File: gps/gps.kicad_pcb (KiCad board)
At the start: 2 copper layers, 167 x 82.5 mm, 62 parts, among them J1 I2C/BATT_H, J12 ENC+RGB, J13 ENC+RGB, J2 I2C/BATT_S, J3 USB_pads, J4 BATT, J5 ESP, J7 USB_B_Micro, J9 USB_pads, SW1 RotaryEncoder_Switch, SW2 SW_DPDT_x2, U1 NEO-M9N, U10 24C32, U2 TPS613222ADBVR, U3 DFR0654, U4 HT16k33, U5 7seg_1x1_rgb, U6 7seg_1x1_rgb, U7 7seg_1x1_rgb, U8 KW4-804AGB

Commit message: tweaks
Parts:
- J7: footprint Connector_USB:USB_Mini-B_Tensility_54-00023_Vertical_CircularHoles -> KiCad:USB3145301A
- REF** (x3): value MountingHole_3.2mm_M3 -> MountingHole_4.3mm_M4; footprint MountingHole:MountingHole_3.2mm_M3 -> MountingHole:MountingHole_4.3mm_M4
- SW2: value SW_DPDT_x2 -> MSN22AFW01
- moved AE1 17.9 mm to (213.8, 105.4), turned to 90 degrees
- moved J3 14.2 mm to (216.8, 95.3), turned to 90 degrees
- moved J5 10.4 mm to (146.7, 61.4), turned to 90 degrees
- moved C3 10.2 mm to (208.6, 101.2), turned to -90 degrees
- moved R_E3 10.1 mm to (63.1, 120.0)
- moved L1 9.90 mm to (208.6, 104.4), turned to 90 degrees
- moved R2 8.00 mm to (206.3, 101.0), turned to -90 degrees
- moved C1 7.34 mm to (193.4, 89.3)
- moved C2 7.34 mm to (189.7, 92.7)
- moved U1 7.34 mm to (197.7, 99.5)
- moved R_E2 6.35 mm to (67.0, 118.3), turned to -90 degrees
- moved R_E1 3.58 mm to (70.9, 109.3)
- moved J7 1.62 mm to (84.3, 49.2)
- moved D2 0.41 mm to (67.7, 70.9)
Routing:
- net SW_ESP: track 147.2 -> 136.9 mm
- net SW: track 88.9 -> 78.7 mm
- net GNSS_RXD: track 55.1 -> 65.0 mm
- net GNSS_TXD: track 44.0 -> 52.1 mm
- net Net-(J3-Pin_2): track 4.73 -> 12.4 mm
- net Net-(U1-VCC_RF): track 2.70 -> 9.01 mm
- net PULSE: track 26.5 -> 31.7 mm
- net Net-(J3-Pin_3): track 5.51 -> 10.7 mm
- net +3V3: track 183.5 -> 187.9 mm
- net CLK: track 77.7 -> 75.6 mm
- net Net-(J3-Pin_4): track 4.90 -> 6.65 mm
- net /Display/aE: track 48.3 -> 49.9 mm
- net Net-(AE1-A): track 8.56 -> 10.2 mm
- net /Display/aCL3: track 44.0 -> 45.5 mm
- net Net-(J7-VBUS): track 19.0 -> 20.4 mm
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
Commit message: tweaks
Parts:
- moved C8 3.38 mm to (204.3, 74.8), turned to -90 degrees
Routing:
- net Net-(J7-D+): track 9.34 -> 12.1 mm
- net +3V3: track 187.9 -> 190.4 mm
- net SDA: track 108.0 -> 109.2 mm
- net GND: vias 384 -> 383

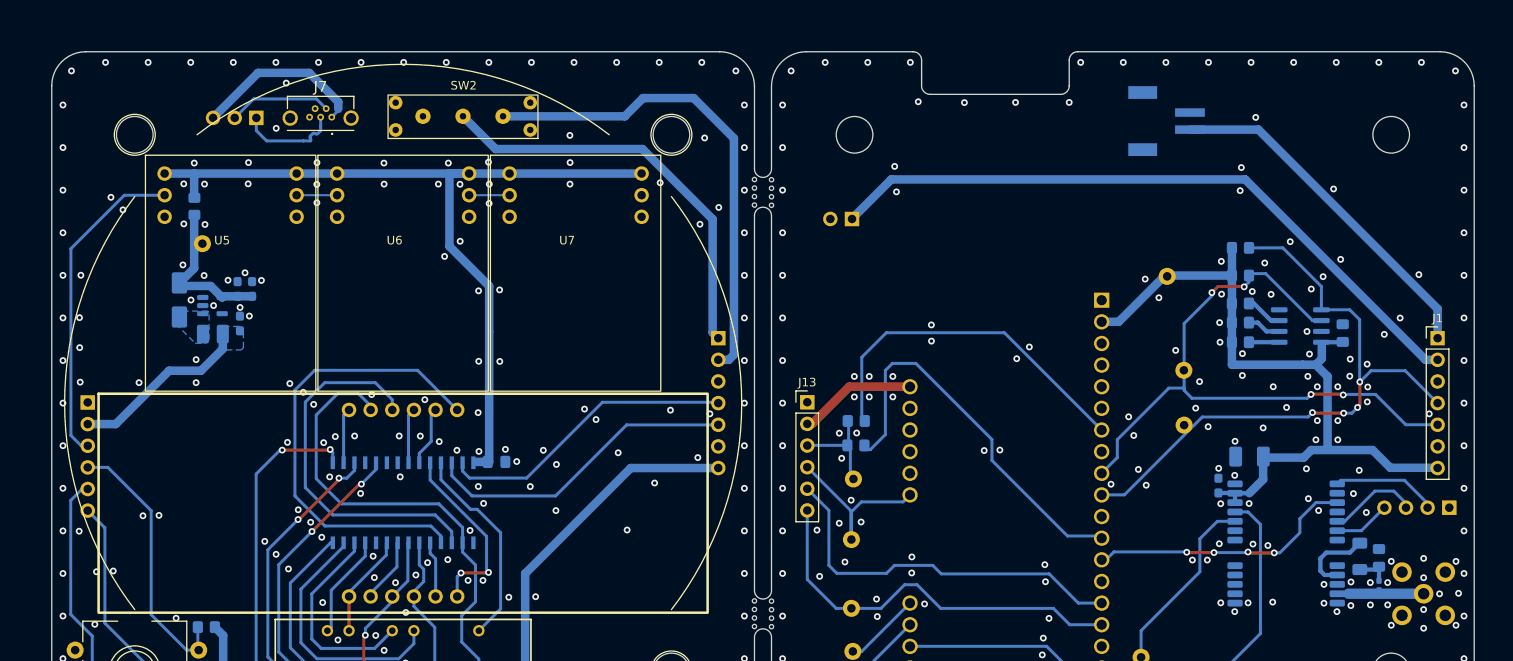
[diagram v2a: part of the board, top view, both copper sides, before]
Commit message: changed eeprom > 5V, RF antenna track corrected to 50ohm
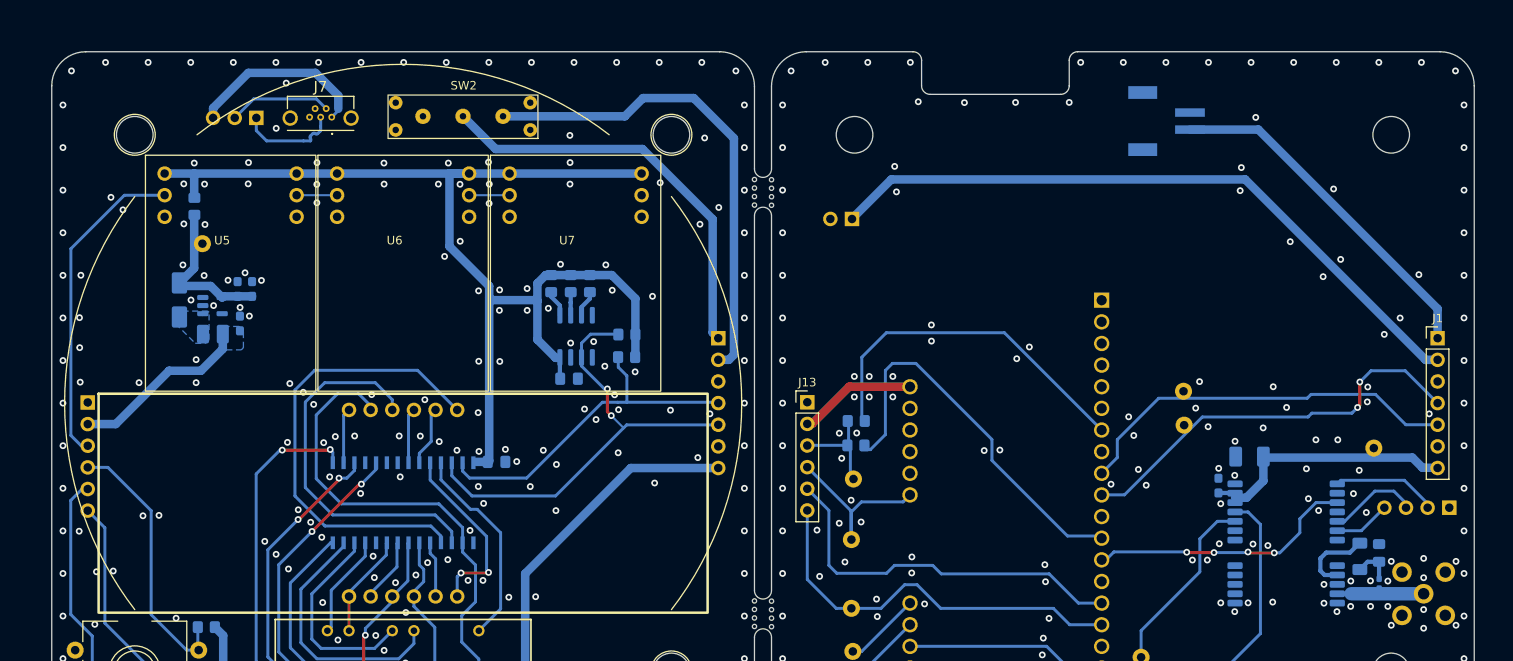
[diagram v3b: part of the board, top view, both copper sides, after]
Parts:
- moved C8 91.0 mm to (113.5, 80.1), turned to 180 degrees
- moved U10 85.0 mm to (114.3, 75.2), turned to -90 degrees
- moved R17 81.2 mm to (111.4, 69.0), turned to -90 degrees
- moved R18 78.8 mm to (113.7, 69.0), turned to -90 degrees
- moved R19 76.4 mm to (115.9, 69.0), turned to -90 degrees
- moved R11 73.2 mm to (120.2, 77.6), turned to 180 degrees
- moved R12 72.4 mm to (120.3, 75.0), turned to 180 degrees
- moved TP7 31.5 mm to (208.0, 88.3)
- moved TP2 2.46 mm to (185.6, 81.6)
- moved C3 0.58 mm to (208.6, 100.6)
- moved L1 0.22 mm to (208.6, 104.2)
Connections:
- C8 pad 2: +3V3 -> +5V
- R11 pad 1: +3V3 -> +5V
- R12 pad 1: +3V3 -> +5V
- R17 pad 1: +3V3 -> +5V
- R18 pad 1: +3V3 -> +5V
- R19 pad 1: +3V3 -> +5V
- U10 pad 8: +3V3 -> +5V
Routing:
- net +3V3: track 190.4 -> 132.3 mm
- net +5V: track 98.5 -> 137.0 mm
- net SDA: track 109.2 -> 90.5 mm, vias 4 -> 2
- net SCL: track 113.6 -> 100.6 mm, vias 4 -> 2
- net Net-(U10-E2): track 4.41 -> 3.12 mm
- net Net-(U10-E1): track 3.98 -> 2.71 mm
- net Net-(J7-VBUS): track 20.4 -> 21.5 mm
- net Net-(C3-Pad2): track 4.03 -> 4.64 mm
- net GND: vias 383 -> 370

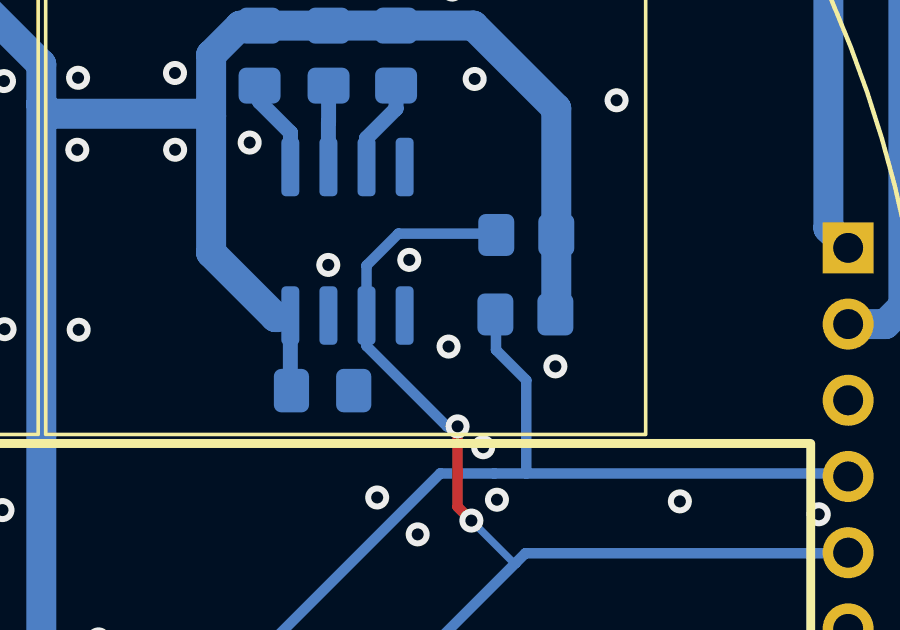
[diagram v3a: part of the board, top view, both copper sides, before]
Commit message: added missing i2c connection
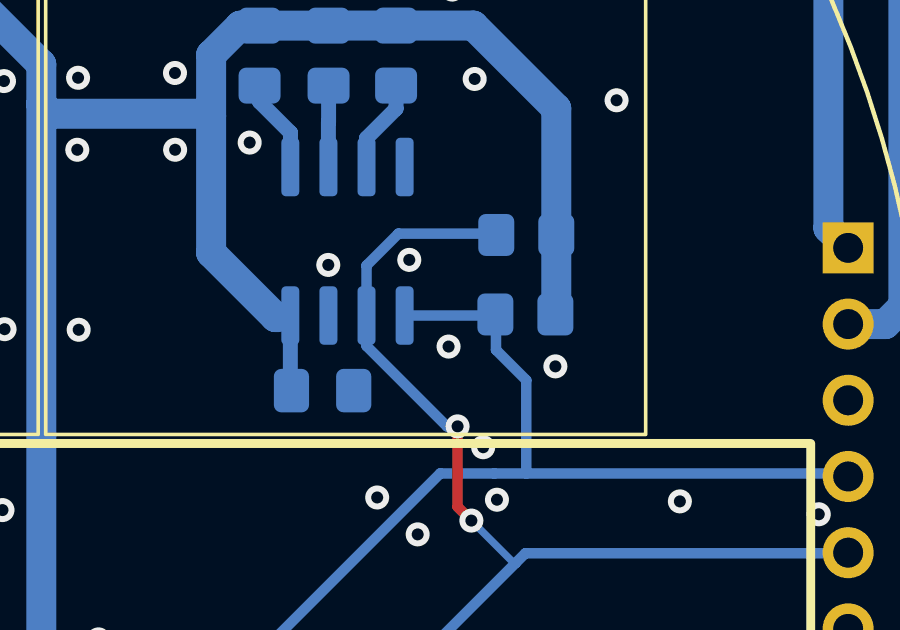
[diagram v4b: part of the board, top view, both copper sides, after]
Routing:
- net SDA: track 90.5 -> 93.6 mm
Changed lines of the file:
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@@
 		(tags "capacitor handsolder")
 		(property "Reference" "C8"
-			(at -1.3 1.78 360)
+			(at -1.3 1.78 0)
 			(layer "B.SilkS")
 			(effects
@@
 		)
 		(property "Value" "100nF"
-			(at -3.448024 0.03 360)
+			(at -3.448024 0.03 0)
 			(layer "B.Fab")
 			(effects
@@
 		)
 		(property "Footprint" "Capacitor_SMD:C_0805_2012Metric_Pad1.18x1.45mm_HandSolder"
-			(at 0 0 360)
+			(at 0 0 0)
 			(layer "F.Fab")
 			(hide yes)
@@
 		)
 		(property "Datasheet" ""
-			(at 0 0 360)
+			(at 0 0 0)
 			(layer "F.Fab")
 			(hide yes)
@@
 		)
 		(property "Description" "Unpolarized capacitor"
-			(at 0 0 360)
+			(at 0 0 0)
 			(layer "F.Fab")
 			(hide yes)
@@
 		)
 		(fp_text user "${REFERENCE}"
-			(at 0 0 360)
+			(at 0 0 0)
 			(layer "B.Fab")
 			(effects
@@
 		(tags "resistor handsolder")
 		(property "Reference" "R12"
-			(at -3.3 0.1 360)
+			(at -3.3 0.1 0)
 			(layer "B.SilkS")
 			(effects
@@
 		)
 		(property "Value" "4k7"
-			(at -3.248024 0.025 360)
+			(at -3.248024 0.025 0)
 			(layer "B.Fab")
 			(effects
@@
 		)
 		(property "Footprint" "Resistor_SMD:R_0805_2012Metric_Pad1.20x1.40mm_HandSolder"
-			(at 0 0 360)
+			(at 0 0 0)
 			(layer "F.Fab")
 			(hide yes)
@@
 		)
 		(property "Datasheet" ""
-			(at 0 0 360)
+			(at 0 0 0)
 			(layer "F.Fab")
 			(hide yes)
@@
 		)
 		(property "Description" "Resistor"
-			(at 0 0 360)
+			(at 0 0 0)
 			(layer "F.Fab")
 			(hide yes)
@@
 		)
 		(fp_text user "${REFERENCE}"
-			(at 0 0 360)
+			(at 0 0 0)
 			(layer "B.Fab")
 			(effects
@@
 		(tags "resistor handsolder")
 		(property "Reference" "R11"
-			(at -3.448024 0.575 360)
+			(at -3.448024 0.575 0)
 			(layer "B.SilkS")
 			(effects
@@
 		)
 		(property "Value" "4k7"
-			(at -3.248024 0.575 360)
+			(at -3.248024 0.575 0)
 			(layer "B.Fab")
 			(effects
@@
 		)
 		(property "Footprint" "Resistor_SMD:R_0805_2012Metric_Pad1.20x1.40mm_HandSolder"
-			(at 0 0 360)
+			(at 0 0 0)
 			(layer "F.Fab")
 			(hide yes)
@@
 		)
 		(property "Datasheet" ""
-			(at 0 0 360)
+			(at 0 0 0)
 			(layer "F.Fab")
 			(hide yes)
@@
 		)
 		(property "Description" "Resistor"
-			(at 0 0 360)
+			(at 0 0 0)
 			(layer "F.Fab")
 			(hide yes)
@@
 		)
 		(fp_text user "${REFERENCE}"
-			(at 0 0 360)
+			(at 0 0 0)
 			(layer "B.Fab")
 			(effects
@@
 	)
 	(segment
+		(start 116.215 77.635)
+		(end 119.205 77.635)
+		(width 0.35)
+		(layer "B.Cu")
+		(net 38)
+	)
+	(segment
 		(start 119.2 82.9)
 		(end 130.89993 82.9)
@@
 		(width 0.35)
 		(layer "B.Cu")
+		(net 38)
+	)
+	(segment
+		(start 119.205 77.635)
+		(end 119.24 77.6)
+		(width 0.35)
+		(layer "B.Cu")

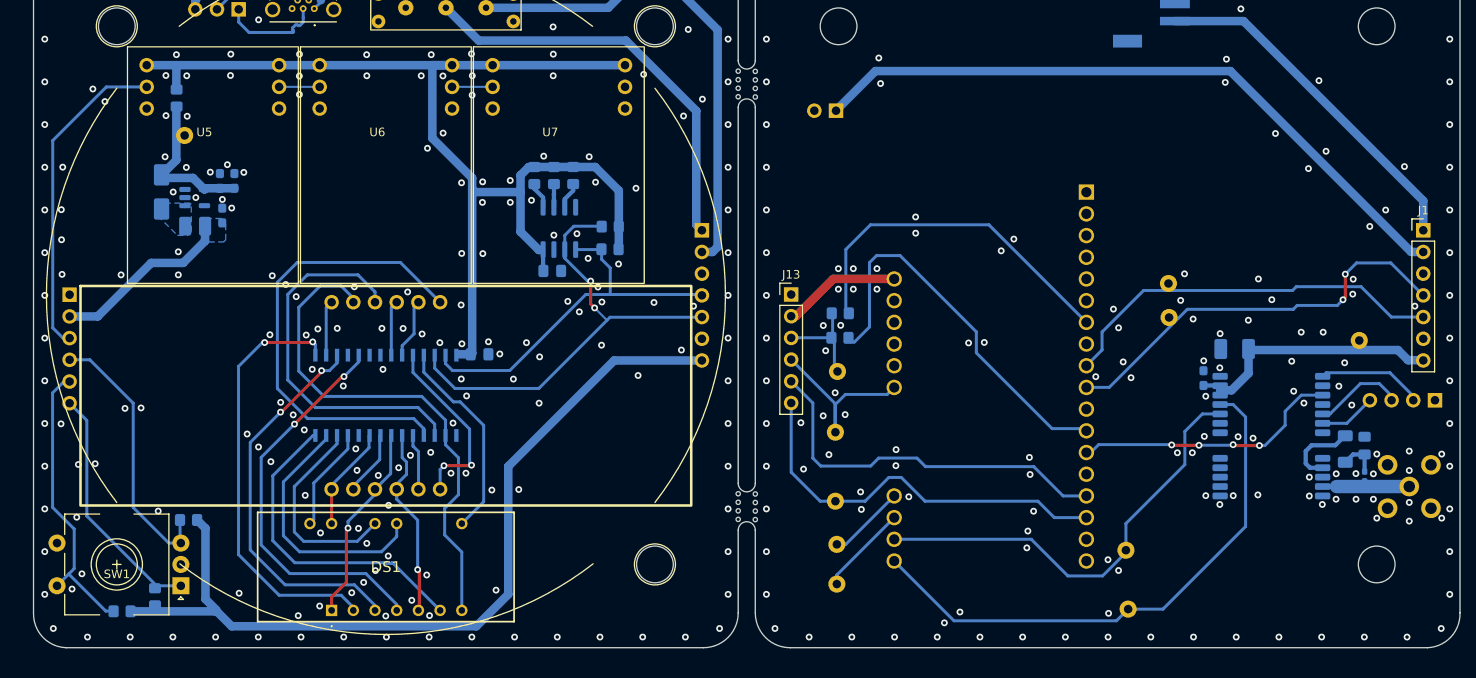
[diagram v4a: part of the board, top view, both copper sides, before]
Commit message: added level shifters for i2C and RGB displey,
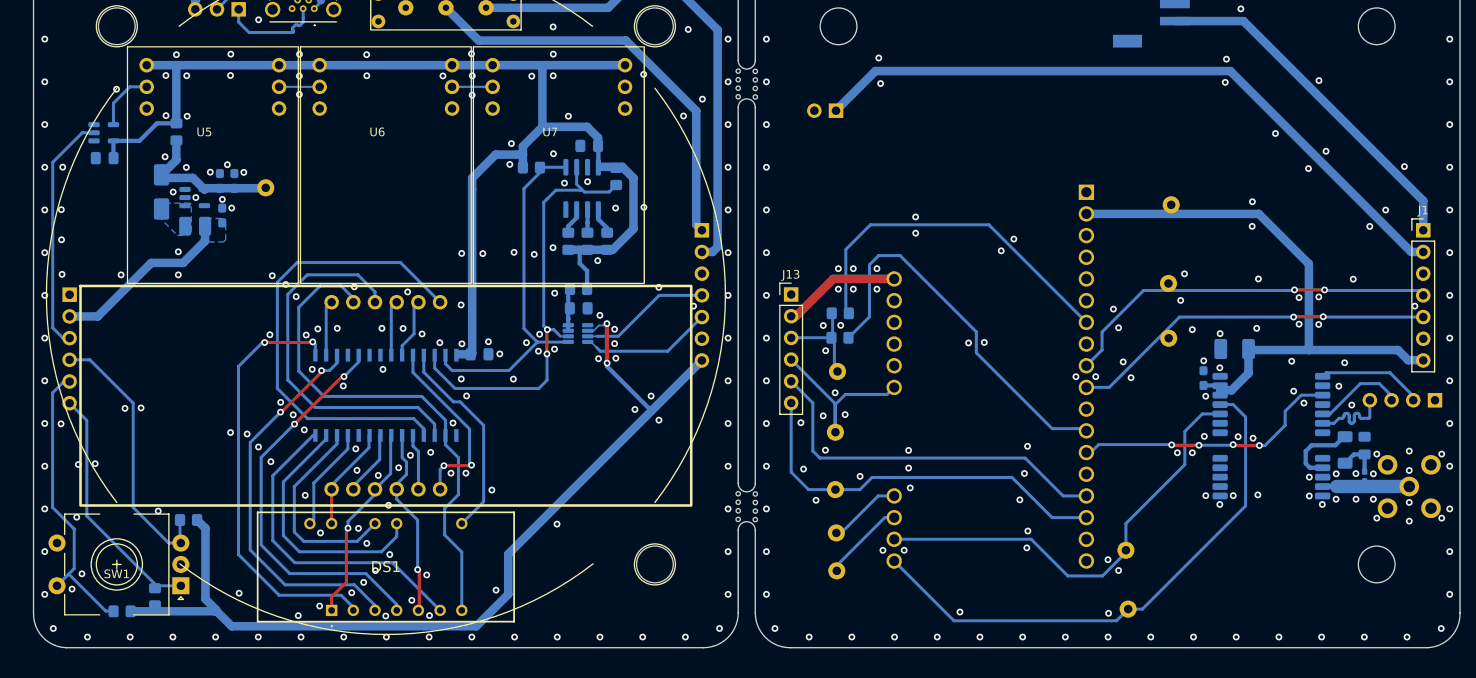
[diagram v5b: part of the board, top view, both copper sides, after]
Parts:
- added C10: 100nF, Capacitor_SMD:C_0805_2012Metric_Pad1.18x1.45mm_HandSolder, B.Cu at (116.6, 84.5)
- added C9: 100nF, Capacitor_SMD:C_0805_2012Metric_Pad1.18x1.45mm_HandSolder, B.Cu at (61.1, 66.9)
- added RS1: 200k, Resistor_SMD:R_0805_2012Metric_Pad1.20x1.40mm_HandSolder, B.Cu at (116.6, 82.3)
- added U11: SN74LV1T34DBVRG4, Package_TO_SOT_SMD:SOT-23-5, B.Cu at (61.0, 64.0)
- added U9: ~, Package_TO_SOT_SMD:SOT-23-8, B.Cu at (116.5, 87.5)
- moved TP7 27.1 mm to (185.9, 72.4)
- moved C8 15.3 mm to (117.8, 65.5), turned to 0 degrees
- moved R11 13.3 mm to (111.0, 68.0), turned to 0 degrees
- moved R17 11.5 mm to (119.9, 76.7), turned to 90 degrees
- moved TP6 11.3 mm to (79.9, 70.4), turned to 0 degrees
- moved R18 8.64 mm to (117.6, 76.7), turned to 90 degrees
- moved R19 7.72 mm to (115.4, 76.7), turned to 90 degrees
- moved R12 5.91 mm to (121.0, 69.1), turned to -90 degrees
- moved U10 5.39 mm to (117.0, 70.5), turned to 90 degrees
- moved R1 3.96 mm to (69.5, 63.9)
- moved TP1 2.43 mm to (185.7, 88.0)
- moved TP13 1.55 mm to (146.8, 115.2)
- moved TP9 1.36 mm to (146.6, 105.7)
- moved TP12 1.34 mm to (146.7, 110.8)
- moved R2 0.11 mm to (206.3, 101.1)
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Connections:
- J1 pad 4: SDA -> SCL_3V3
- J1 pad 5: SCL -> SDA_3V3
- J12 pad 3: RGB_7seg -> RGB_3V3
- J13 pad 3: RGB_7seg -> RGB_3V3
- J2 pad 4: SDA -> SCL_3V3
- J2 pad 5: SCL -> SDA_3V3
- R11 pad 2: SDA -> SDA_5V
- R12 pad 2: SCL -> SCL_5V
- TP1 pad 1: SDA -> SDA_3V3
- TP10 pad 1: RGB_7seg -> Net-(U3-MOSI)
- TP10 pad 2: Net-(U3-MOSI) -> RGB_3V3
- TP11 pad 2: RGB_7seg -> RGB_3V3
- TP2 pad 1: SCL -> SCL_3V3
- TP3 pad 1: RGB_7seg -> RGB_3V3
- U10 pad 5: SDA -> SDA_5V
- U10 pad 6: SCL -> SCL_5V
- U3 pad 10: SDA -> SDA_3V3
- U3 pad 28: SDA -> SDA_3V3
- U3 pad 29: SCL -> SCL_3V3
- U3 pad 9: SCL -> SCL_3V3
- U4 pad 26: SCL -> SCL_5V
- U4 pad 27: SDA -> SDA_5V
- U5 pad 2: RGB_7seg -> RGB_5V
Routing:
- net SCL: track 100.6 -> 0.00 mm, vias 2 -> 0
- net SDA: track 93.6 -> 0.00 mm, vias 2 -> 0
- net SCL_3V3: track 0.00 -> 60.2 mm, vias 0 -> 2
- net SDA_3V3: track 0.00 -> 58.7 mm, vias 0 -> 2
- net SCL_5V: track 0.00 -> 52.3 mm, vias 0 -> 2
- net RGB_7seg: track 50.3 -> 0.00 mm
- net +3V3: track 132.3 -> 179.8 mm, vias 0 -> 2
- net SDA_5V: track 0.00 -> 42.0 mm
- net RGB_3V3: track 0.00 -> 40.4 mm
- net +5V: track 137.0 -> 150.2 mm
- net RGB_5V: track 0.00 -> 7.19 mm
- net Net-(U9-EN): track 0.00 -> 3.98 mm
- net Net-(J3-Pin_4): track 6.65 -> 10.4 mm
- net Net-(U3-D7): track 46.8 -> 45.3 mm
- net GNSS_RXD: track 65.0 -> 63.6 mm
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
